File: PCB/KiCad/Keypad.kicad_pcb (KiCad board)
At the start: 2 copper layers, 77 x 132.8 mm, 17 parts, among them SW1 SW_SPDT, U1 TP4056, U2 MT3608, U3 WeMos_D1_mini

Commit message: kicad files updated.
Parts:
- added R6: 500K, Resistor_THT:R_Axial_DIN0207_L6.3mm_D2.5mm_P10.16mm_Horizontal, F.Cu at (130.6, 127.8)
- added U4: MCP3421A0T-ECH, Package_TO_SOT_SMD:SOT-23-6_Handsoldering, F.Cu at (138.2, 128.0)
- BT1: value 3.7V Li-ion Battery -> 3.7V LiPo Battery
- Keypad1: value Conn_01x09 -> Conn_01x03; footprint Connector_PinHeader_2.54mm:PinHeader_1x09_P2.54mm_Vertical -> Connector_PinHeader_2.54mm:PinHeader_1x03_P2.54mm_Vertical
- R5: value 100k -> 560k
- SW1: value SW_SPDT -> SW_DIP_x01; footprint Button_Switch_THT:SW_Slide_1P2T_CK_OS102011MS2Q -> Keypad:Mini_Latching_Torch_Switch
- moved Keypad1 12.6 mm to (147.1, 147.8), turned to 270 degrees
- moved SW1 7.81 mm to (115.3, 145.5), turned to 90 degrees
- moved D1 5.75 mm to (132.0, 31.8)
- moved D2 5.75 mm to (126.3, 31.8)
- moved D3 5.75 mm to (119.9, 31.8)
- moved DS1 5.61 mm to (181.7, 40.0)
- moved U1 1.00 mm to (175.5, 136.2)
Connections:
- D1 pad 1: /LED_Control1 -> GND
- D2 pad 1: /LED_Control2 -> GND
- Keypad1 pad 1: Net-(Keypad1-Pad1) -> keypad
- Keypad1 pad 2: /KP1 -> GND
- Keypad1 pad 3: /KP2 -> +3V3
- R1 pad 1: +3V3 -> red
- R2 pad 1: /LED_Control1 -> yellow
- R3 pad 1: /LED_Control2 -> green
- SW1 pad 1: /V+2 -> /V+1
- SW1 pad 2: /V+1 -> Net-(SW1-Pad2)
- U2 pad 1: /V+2 -> Net-(SW1-Pad2)
- U3 pad 11: /KP1 -> Net-(U3-Pad11)
- U3 pad 12: /KP2 -> Net-(U3-Pad12)
- U3 pad 15: /LED_Control2 -> Net-(U3-Pad15)
- U3 pad 16: /LED_Control1 -> Net-(U3-Pad16)
- U3 pad 2: Net-(R5-Pad2) -> keypad
- U3 pad 3: /KP7 -> Net-(U3-Pad3)
- U3 pad 4: /KP6 -> Net-(U3-Pad4)
- U3 pad 5: /KP5 -> red
- U3 pad 6: /KP4 -> yellow
- U3 pad 7: /KP3 -> green
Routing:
- net /LED_Control1: track 71.5 -> 0.00 mm
- net /LED_Control2: track 68.2 -> 0.00 mm
- net /KP1: track 61.0 -> 0.00 mm
- net /KP2: track 60.5 -> 0.00 mm
- net /V+2: track 55.7 -> 0.00 mm
- net Net-(SW1-Pad2): track 0.00 -> 53.1 mm
- net SDA: track 66.0 -> 116.4 mm
- net green: track 0.00 -> 48.5 mm
- net yellow: track 0.00 -> 39.9 mm
- net SCL: track 70.1 -> 109.8 mm, vias 0 -> 1
- net keypad: track 0.00 -> 37.0 mm
- net /KP7: track 34.5 -> 0.00 mm
- net /KP6: track 34.5 -> 0.00 mm
- net /KP4: track 34.5 -> 0.00 mm
- net /KP3: track 34.5 -> 0.00 mm
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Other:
- board size 77 x 132.8 mm -> 79 x 137.9 mm

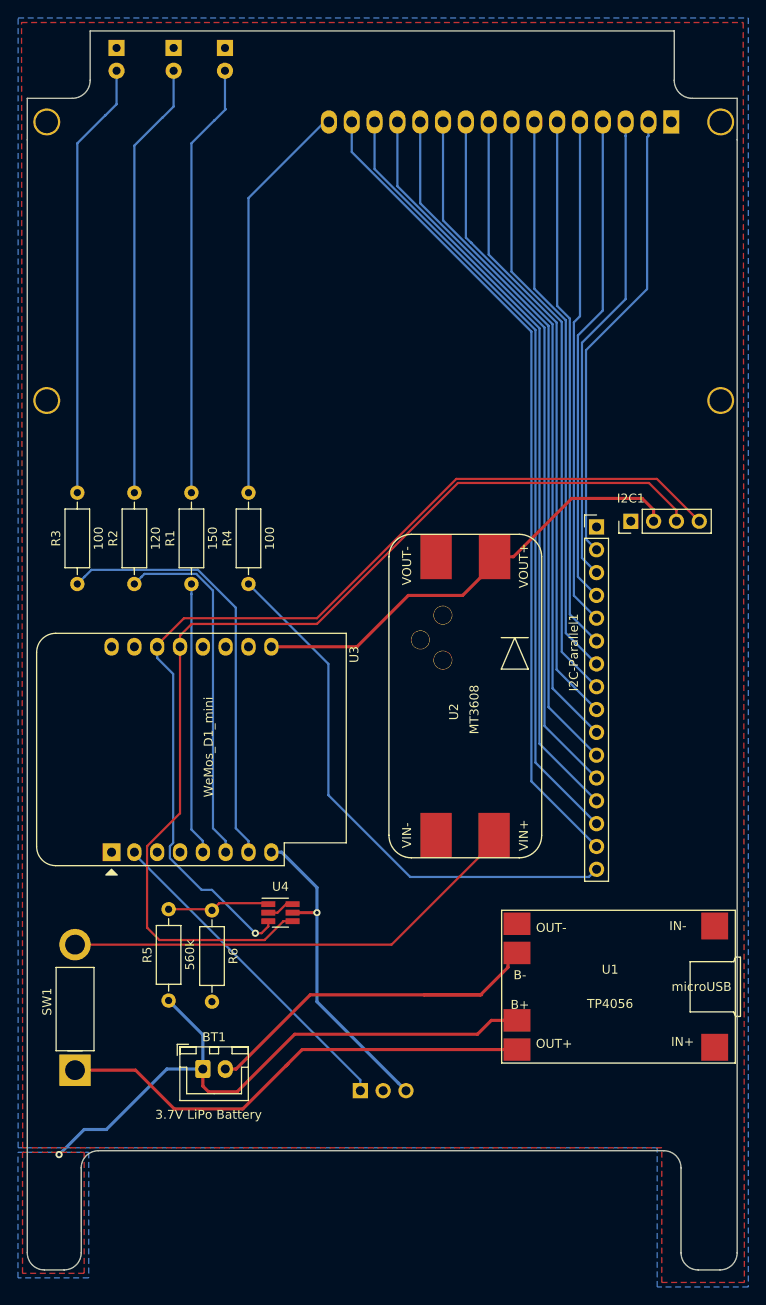
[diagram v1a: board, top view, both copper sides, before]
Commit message: adjustments
LCD moved 2mm in. Wemos rotated 180. 100uF cap added.
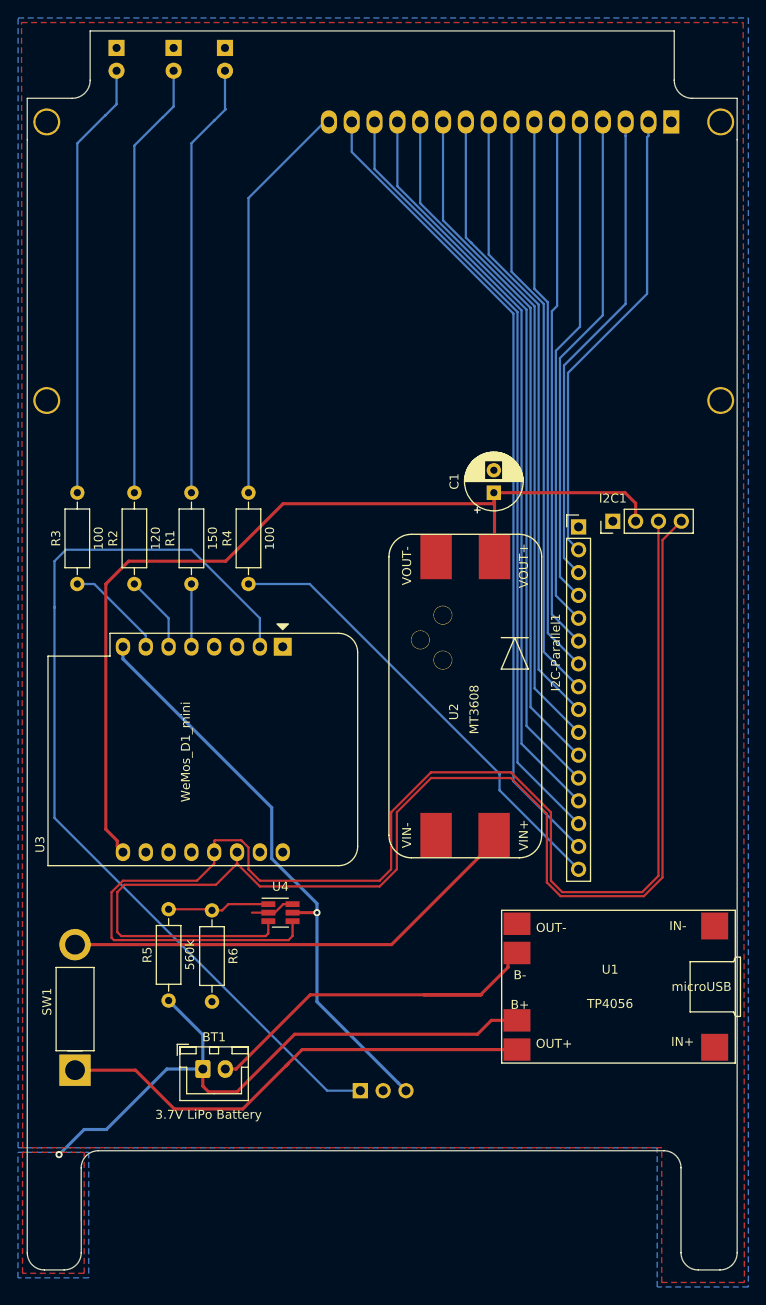
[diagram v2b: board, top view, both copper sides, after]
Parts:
- added C1: 100u, Capacitor_THT:CP_Radial_D6.3mm_P2.50mm, F.Cu at (161.9, 81.3)
- moved U3 29.8 mm to (138.4, 98.4), turned to 270 degrees
- moved I2C-Parallel1 2.00 mm to (171.4, 85.1)
- moved I2C1 2.00 mm to (175.2, 84.5)
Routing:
- net keypad: track 37.0 -> 105.0 mm
- net +5V: track 51.6 -> 104.1 mm
- net SDA: track 116.4 -> 154.1 mm
- net SCL: track 109.8 -> 147.2 mm, vias 1 -> 0
- net green: track 48.5 -> 11.7 mm
- net yellow: track 39.9 -> 8.56 mm
- net +3V3: track 36.3 -> 65.2 mm
- net red: track 30.6 -> 6.98 mm
- net /LCD16: track 61.1 -> 51.0 mm
- net GND: track 3.09 -> 4.92 mm
- net /LCD9: track 70.4 -> 69.5 mm
- net /LCD8: track 66.8 -> 65.9 mm
- net /LCD15: track 91.9 -> 91.1 mm
- net /LCD14: track 88.3 -> 87.5 mm
- net /LCD4: track 54.7 -> 55.5 mm
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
